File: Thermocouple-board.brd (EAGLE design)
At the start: 76.2 x 99.1 mm, 107 parts, among them J1 RJ45, J10 1X2-3.5MM, J11 1X2-3.5MM, J12 1X2-3.5MM, J13 1X2-3.5MM, J2 RJ45, J20 HEADER-1X1, J21 HEADER-1X1, J22 HEADER-1X1, J3 1981584-1LONGPADS, J4 2.1MMJACKTHM, J5 ST-LINK, J6 HEADER-1X3, J7 UART, SW1 PUSHBUTTON, SW2 PUSHBUTTON, U1 STM32F042K6, U10 MAX31855, U11 MAX31855, U12 MAX31855, U13 MAX31855, U20 EEPROM-I2C, U21 EEPROM-I2C, U30 ST3485, U31 ST3485, U40 LP298XS, U70 TPS25921, Y1 8MHz

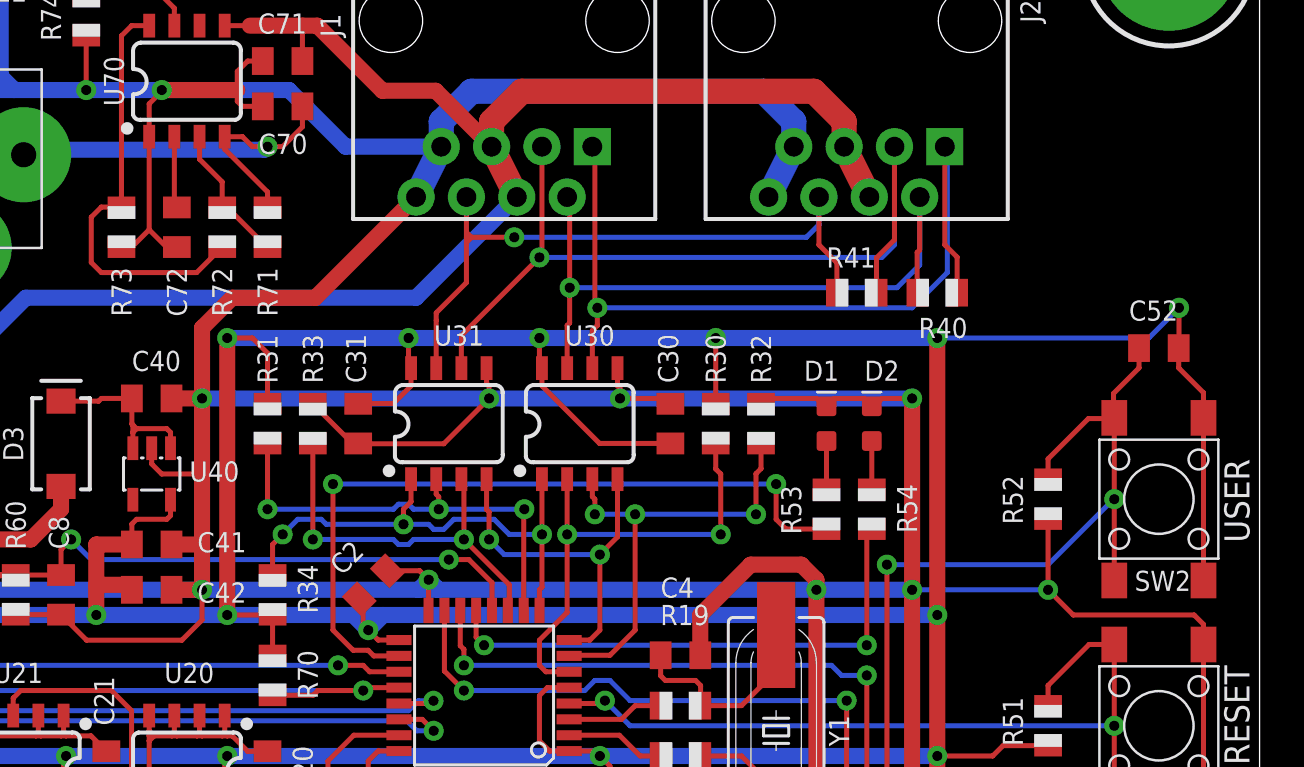
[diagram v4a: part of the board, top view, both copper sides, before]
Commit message: Moved LEDs to uper right corner
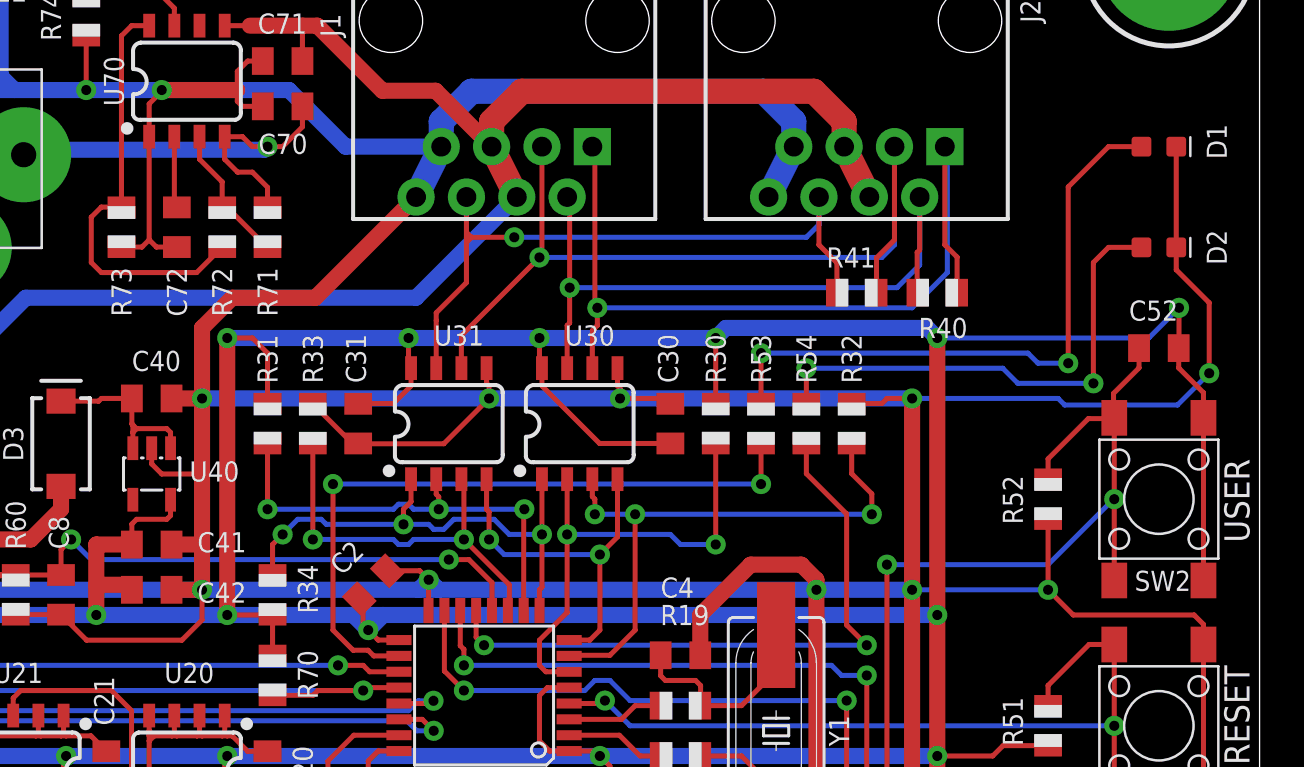
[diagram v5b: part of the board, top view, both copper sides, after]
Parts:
- moved D1 21.8 mm to (71.1, 85.1), turned to 0 degrees
- moved D2 17.0 mm to (71.1, 80.0), turned to 0 degrees
- moved R53 5.44 mm to (51.1, 71.1)
- moved R54 5.44 mm to (53.3, 71.1)
- moved R32 4.57 mm to (55.6, 71.1)
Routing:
- net N$25: track 2.44 -> 31.7 mm, vias 0 -> 2
- net GND: track 663.4 -> 686.6 mm, vias 30 -> 31
- net N$26: track 2.44 -> 25.4 mm, vias 0 -> 2
- net UART2_DE1: track 23.3 -> 29.5 mm
- net LED_RED: track 27.2 -> 32.7 mm
- net LED_GRN: track 38.1 -> 34.9 mm

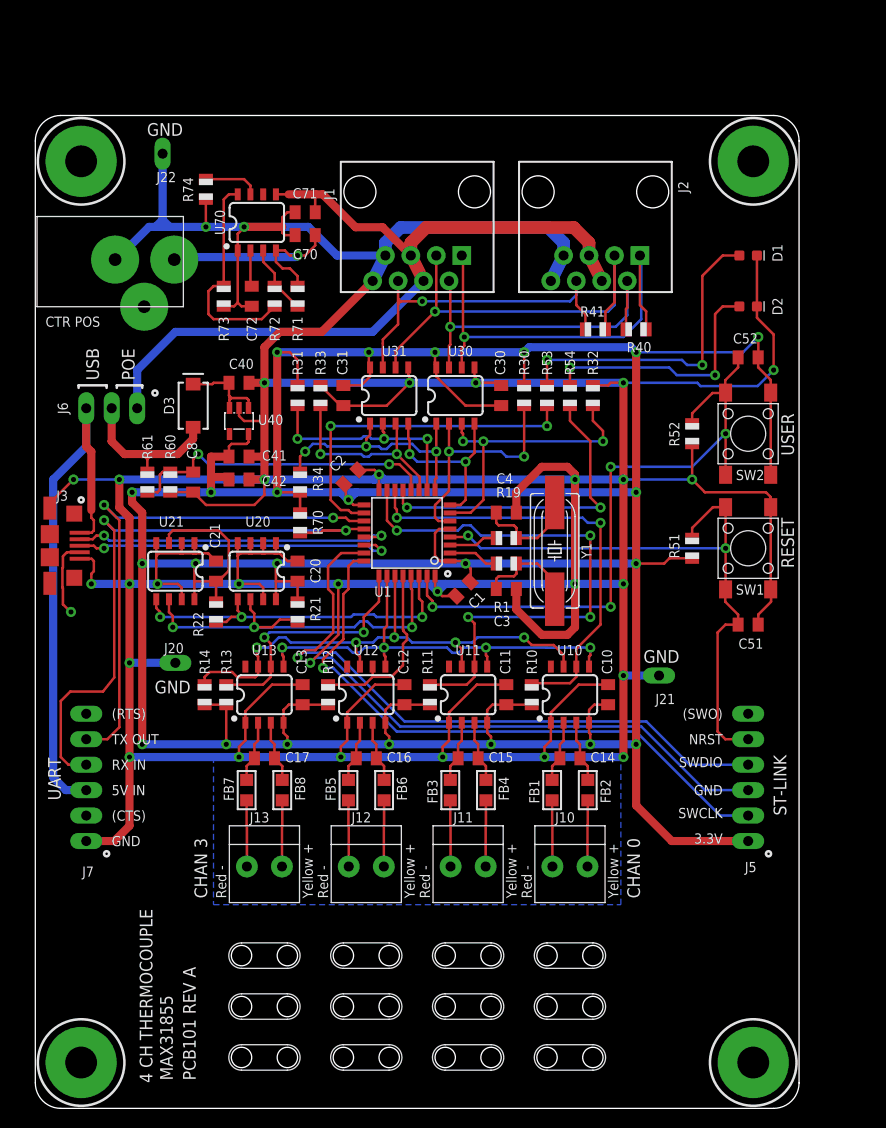
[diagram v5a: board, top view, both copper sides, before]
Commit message: Reroute efuse
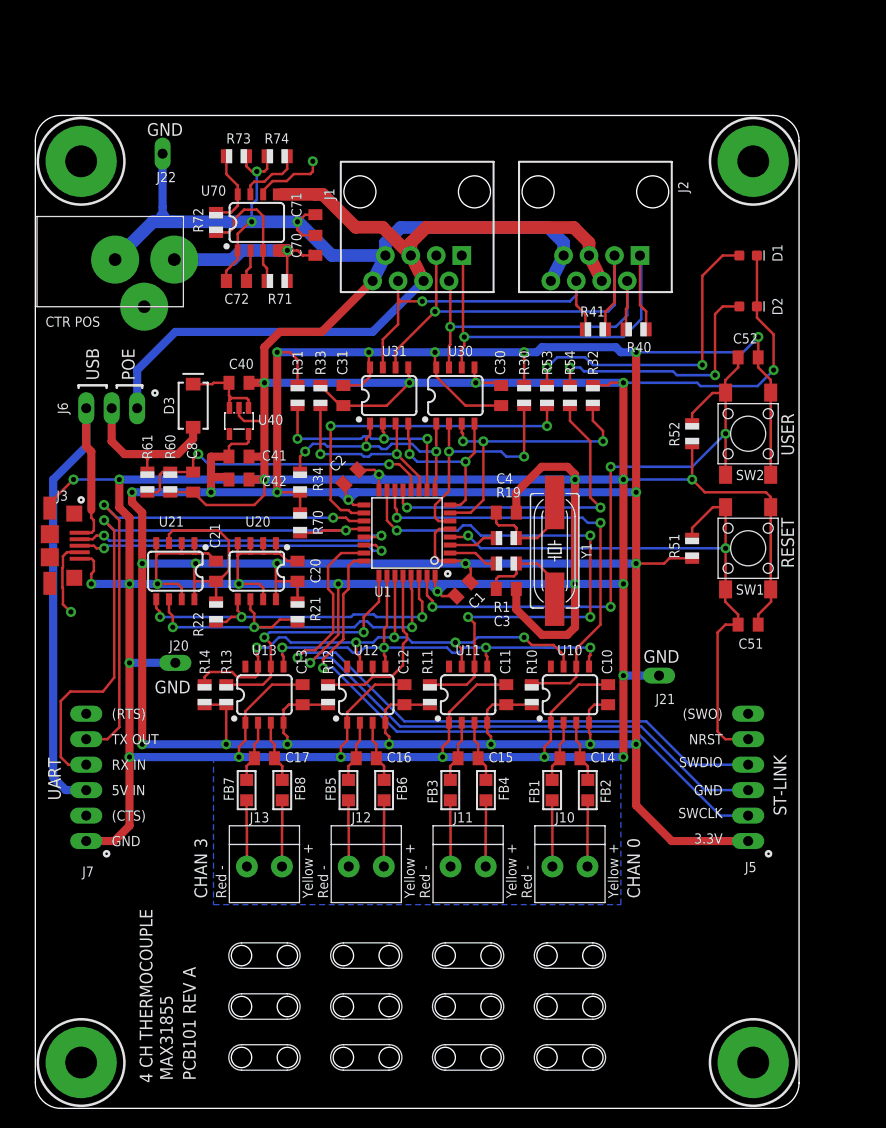
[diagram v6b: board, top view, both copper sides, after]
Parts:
- moved R73 14.0 mm to (20.1, 95.0), turned to 0 degrees
- moved R72 9.40 mm to (18.0, 88.4), turned to 90 degrees
- moved R74 7.84 mm to (24.1, 95.0), turned to 180 degrees
- moved R71 2.54 mm to (24.1, 82.5), turned to 180 degrees
- moved C72 2.16 mm to (20.1, 82.5), turned to 180 degrees
- moved C70 1.44 mm to (27.9, 86.1), turned to 90 degrees
- moved C71 1.27 mm to (27.9, 90.2), turned to 270 degrees
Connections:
- net N$23 renamed UV
- net N$24 renamed OVP
- net N$27 renamed ILIM
- net N$28 renamed SS
- new net FLT_N: U70.6
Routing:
- net OVP: track 21.6 -> 7.85 mm
- net FLT_N: track 0.00 -> 7.13 mm, vias 0 -> 1
- net UV: track 7.15 -> 13.0 mm
- net PWR_SRC: track 22.9 -> 19.6 mm
- net POE_PWR: track 81.1 -> 79.4 mm
- net GND: track 686.6 -> 688.1 mm, vias 31 -> 32
- net ILIM: track 5.60 -> 6.50 mm

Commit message: Routing complete
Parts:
- moved MH1 0.72 mm to (5.08, 5.08)
- moved MH2 0.72 mm to (71.1, 5.08)
- moved MH3 0.72 mm to (5.08, 94.0)
- moved MH4 0.72 mm to (71.1, 94.0)
- moved C8 0.25 mm to (16.0, 62.5)
- moved R60 0.25 mm to (13.7, 62.5)
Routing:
- net GND: track 688.1 -> 701.2 mm
- net POE_PWR: track 79.4 -> 81.9 mm
- net +3V3: track 434.4 -> 436.5 mm
- net PWR_SRC: track 19.6 -> 18.9 mm

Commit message: Update values on schematic
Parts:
- C70: value 10pF -> 1uF
- C71: value 10pF -> 10uF
- C72: value 10pF -> 0.1uF
- R61: value 10K -> 30.1K
- R71: value 10K -> 73.2K
- R72: value 10K -> 22.1K
- R73: value 10K -> 11.5K
- R74: value 10K -> 93.1K
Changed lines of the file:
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@@
 <attribute name="VALUE" x="11.43" y="63.246" size="1.27" layer="27" rot="R270"/>
 </element>
-<element name="R61" library="adafruit" package="R0805" value="10K" x="11.176" y="62.484" smashed="yes" rot="R270">
+<element name="R61" library="adafruit" package="R0805" value="30.1K" x="11.176" y="62.484" smashed="yes" rot="R270">
 <attribute name="NAME" x="11.684" y="64.77" size="1.016" layer="25" font="vector" ratio="15" rot="R90"/>
 <attribute name="VALUE" x="8.89" y="63.246" size="1.27" layer="27" rot="R270"/>
@@
 <attribute name="VALUE" x="25.908" y="88.392" size="0.6096" layer="27" font="vector" ratio="20" rot="R90" align="bottom-center"/>
 </element>
-<element name="R71" library="adafruit" package="R0805" value="10K" x="24.13" y="82.55" smashed="yes" rot="R180">
+<element name="R71" library="adafruit" package="R0805" value="73.2K" x="24.13" y="82.55" smashed="yes" rot="R180">
 <attribute name="NAME" x="25.654" y="81.28" size="1.016" layer="25" font="vector" ratio="15" rot="R180"/>
 <attribute name="VALUE" x="24.892" y="84.836" size="1.27" layer="27" rot="R180"/>
 </element>
-<element name="R72" library="adafruit" package="R0805" value="10K" x="18.034" y="88.392" smashed="yes" rot="R90">
+<element name="R72" library="adafruit" package="R0805" value="22.1K" x="18.034" y="88.392" smashed="yes" rot="R90">
 <attribute name="NAME" x="16.764" y="87.376" size="1.016" layer="25" font="vector" ratio="15" rot="R90"/>
 <attribute name="VALUE" x="20.32" y="87.63" size="1.27" layer="27" rot="R90"/>
 </element>
-<element name="R73" library="adafruit" package="R0805" value="10K" x="20.066" y="94.996" smashed="yes">
+<element name="R73" library="adafruit" package="R0805" value="11.5K" x="20.066" y="94.996" smashed="yes">
 <attribute name="NAME" x="19.05" y="96.266" size="1.016" layer="25" font="vector" ratio="15"/>
 <attribute name="VALUE" x="19.304" y="92.71" size="1.27" layer="27"/>
 </element>
-<element name="R74" library="adafruit" package="R0805" value="10K" x="24.13" y="94.996" smashed="yes" rot="R180">
+<element name="R74" library="adafruit" package="R0805" value="93.1K" x="24.13" y="94.996" smashed="yes" rot="R180">
 <attribute name="NAME" x="22.86" y="96.266" size="1.016" layer="25" font="vector" ratio="15"/>
 <attribute name="VALUE" x="24.892" y="97.282" size="1.27" layer="27" rot="R180"/>
 </element>
-<element name="C72" library="adafruit" library_urn="urn:adsk.eagle:library:420" package="C0805K" package3d_urn="urn:adsk.eagle:package:6240397/1" value="10pF" x="20.066" y="82.55" smashed="yes" rot="R180">
+<element name="C72" library="adafruit" library_urn="urn:adsk.eagle:library:420" package="C0805K" package3d_urn="urn:adsk.eagle:package:6240397/1" value="0.1uF" x="20.066" y="82.55" smashed="yes" rot="R180">
 <attribute name="NAME" x="21.336" y="81.28" size="1.016" layer="25" font="vector" ratio="15" rot="R180"/>
 <attribute name="VALUE" x="21.066" y="84.45" size="1.016" layer="27" rot="R180"/>
 </element>
-<element name="C71" library="adafruit" library_urn="urn:adsk.eagle:library:420" package="C0805K" package3d_urn="urn:adsk.eagle:package:6240397/1" value="10pF" x="27.94" y="90.17" smashed="yes" rot="R270">
+<element name="C71" library="adafruit" library_urn="urn:adsk.eagle:library:420" package="C0805K" package3d_urn="urn:adsk.eagle:package:6240397/1" value="10uF" x="27.94" y="90.17" smashed="yes" rot="R270">
 <attribute name="NAME" x="26.557" y="88.916" size="1.016" layer="25" font="vector" ratio="15" rot="R90"/>
 <attribute name="VALUE" x="26.04" y="91.17" size="1.016" layer="27" rot="R270"/>
@@
 <attribute name="VALUE" x="55.118" y="75.438" size="1.27" layer="27"/>
 </element>
-<element name="C70" library="adafruit" library_urn="urn:adsk.eagle:library:420" package="C0805K" package3d_urn="urn:adsk.eagle:package:6240397/1" value="10pF" x="27.94" y="86.106" smashed="yes" rot="R90">
+<element name="C70" library="adafruit" library_urn="urn:adsk.eagle:library:420" package="C0805K" package3d_urn="urn:adsk.eagle:package:6240397/1" value="1uF" x="27.94" y="86.106" smashed="yes" rot="R90">
 <attribute name="NAME" x="26.557" y="84.852" size="1.016" layer="25" font="vector" ratio="15" rot="R90"/>
 <attribute name="VALUE" x="29.84" y="85.106" size="1.016" layer="27" rot="R90"/>
